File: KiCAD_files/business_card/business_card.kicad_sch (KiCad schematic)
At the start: 74 parts, among them J1 USB_C_Receptacle_USB2.0_14P, SW1 SW_MEC_5G, SW2 SW_MEC_5G, SW3 SW_MEC_5G, SW4 SW_MEC_5G, SW5 SW_MEC_5G, SW6 SW_MEC_5G, SW7 SW_MEC_5G, SW8 SW_MEC_5G, U1 STM32U073CCUx, U2 MCP1700x-300xxTT, U3 TPS3839DBZ

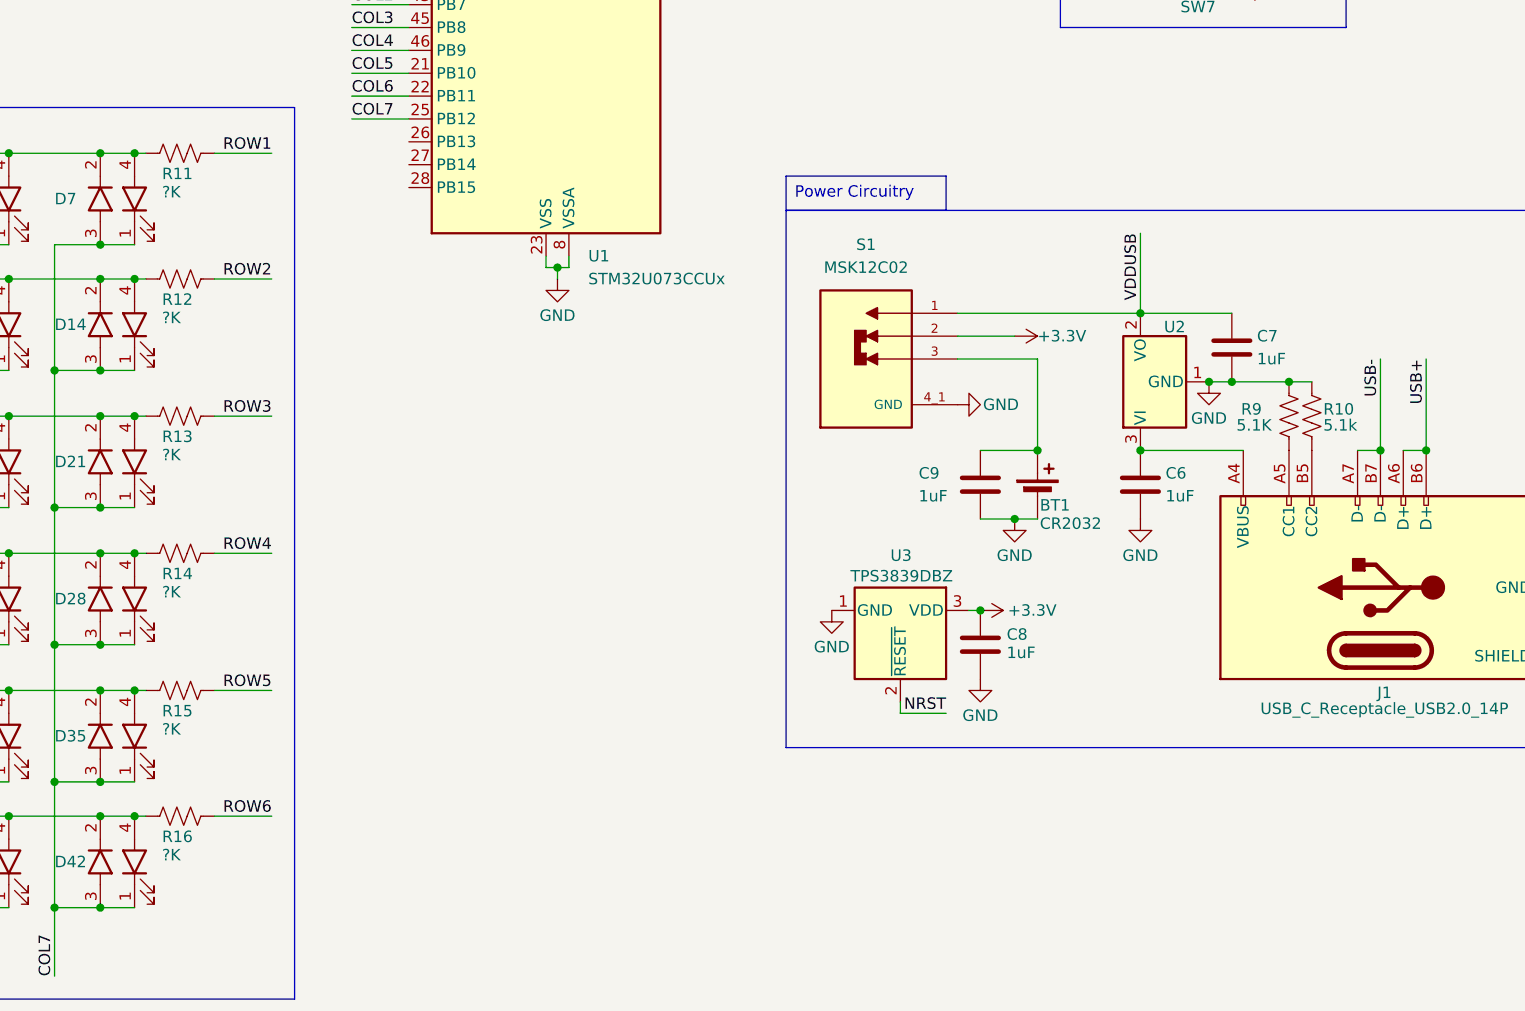
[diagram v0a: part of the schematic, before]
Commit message: Clean Up Files and Add Footprints
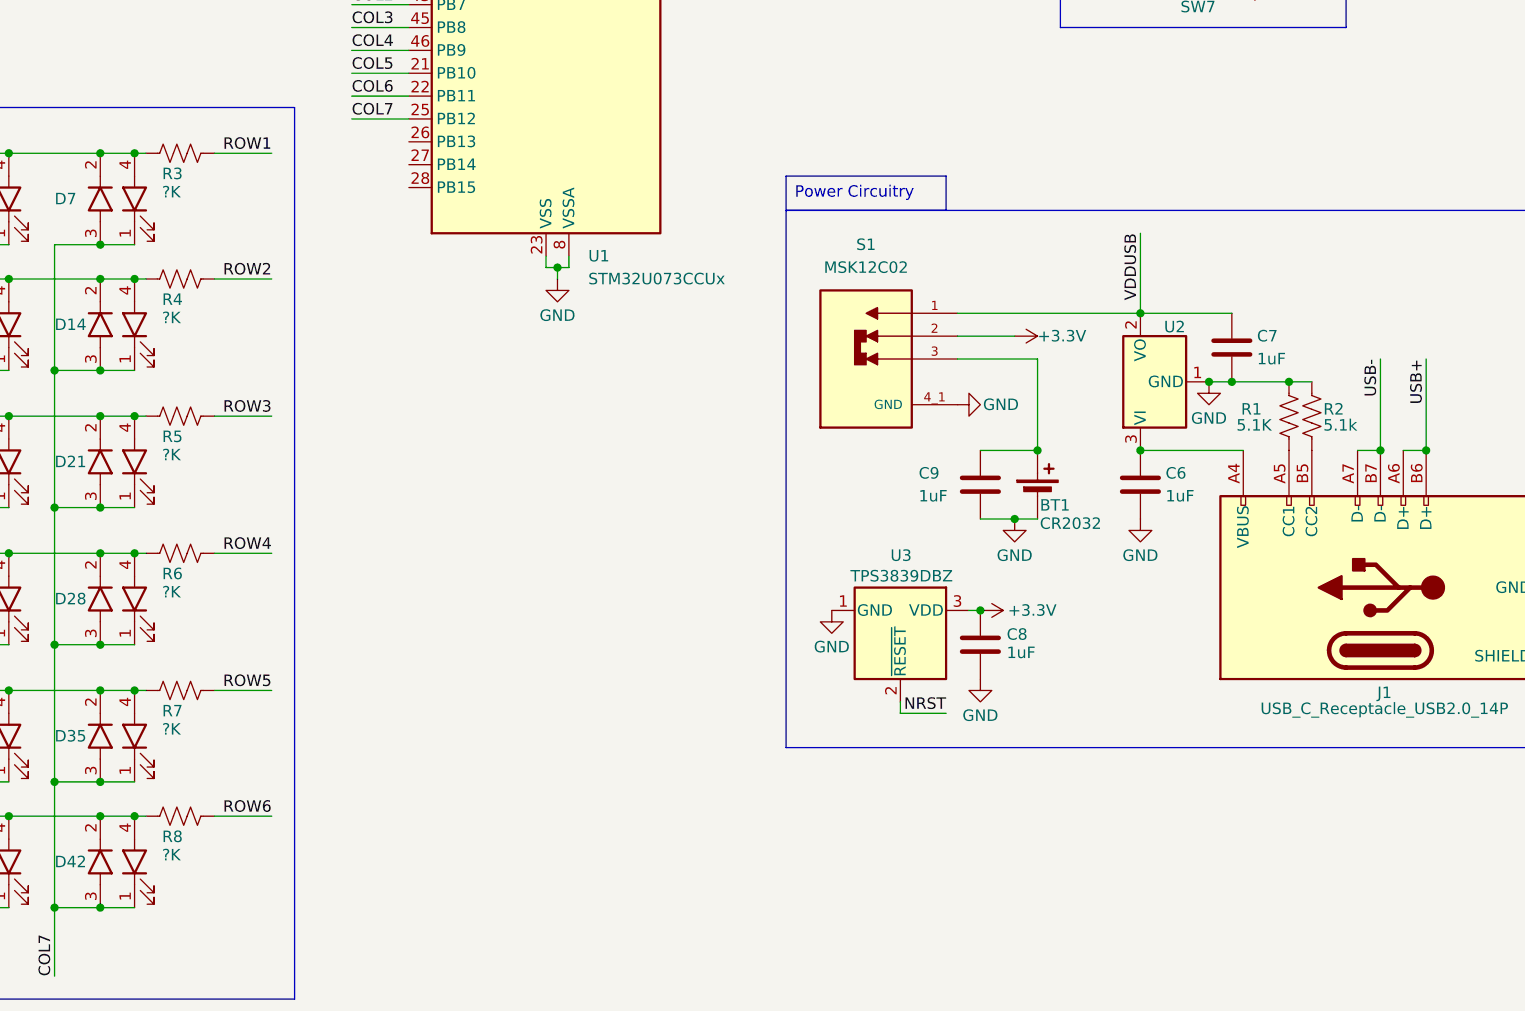
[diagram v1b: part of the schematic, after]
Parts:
- BT1: footprint (none) -> Battery:BatteryHolder_Keystone_3002_1x2032
- C1, C2, C3, C4, C5, C6, C7, C8, C9: footprint (none) -> Capacitor_SMD:C_0603_1608Metric
- R1: renamed from R9; footprint (none) -> Resistor_SMD:R_0603_1608Metric
- R2: renamed from R10; footprint (none) -> Resistor_SMD:R_0603_1608Metric
- R3: renamed from R11; footprint (none) -> Resistor_SMD:R_0603_1608Metric
- R4: renamed from R12; footprint (none) -> Resistor_SMD:R_0603_1608Metric
- R5: renamed from R13; footprint (none) -> Resistor_SMD:R_0603_1608Metric
- R6: renamed from R14; footprint (none) -> Resistor_SMD:R_0603_1608Metric
- R7: renamed from R15; footprint (none) -> Resistor_SMD:R_0603_1608Metric
- R8: renamed from R16; footprint (none) -> Resistor_SMD:R_0603_1608Metric
- SW1, SW2, SW3, SW4, SW5, SW6, SW7: footprint (none) -> custom_footprints:TSB008A2518A
- SW8: footprint (none) -> custom_footprints:TVAF06-N020C2-R
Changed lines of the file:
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@@
 			)
 		)
-		(property "Footprint" ""
+		(property "Footprint" "custom_footprints:TSB008A2518A"
 			(at 233.68 73.66 0)
 			(effects
@@
 		(on_board yes)
 		(dnp no)
-		(property "Reference" "R15"
+		(property "Reference" "R7"
 			(at 118.618 158.496 90)
 			(effects
@@
 			)
 		)
-		(property "Footprint" ""
+		(property "Footprint" "Resistor_SMD:R_0603_1608Metric"
 			(at 120.904 155.194 90)
 			(effects
@@
 			(project "business_card"
 				(path "/16d1a3fe-4f2d-4eb3-9740-21c0af2e4feb"
-					(reference "R15")
+					(reference "R7")
 					(unit 1)
 				)
@@
 		(on_board yes)
 		(dnp no)
-		(property "Reference" "R11"
+		(property "Reference" "R3"
 			(at 118.618 98.806 90)
 			(effects
@@
 			)
 		)
-		(property "Footprint" ""
+		(property "Footprint" "Resistor_SMD:R_0603_1608Metric"
 			(at 120.904 95.504 90)
 			(effects
@@
 			(project "business_card"
 				(path "/16d1a3fe-4f2d-4eb3-9740-21c0af2e4feb"
-					(reference "R11")
+					(reference "R3")
 					(unit 1)
 				)
@@
 			)
 		)
-		(property "Footprint" ""
+		(property "Footprint" "Capacitor_SMD:C_0603_1608Metric"
 			(at 228.2952 137.16 0)
 			(effects
@@
 			)
 		)
-		(property "Footprint" ""
+		(property "Footprint" "custom_footprints:TSB008A2518A"
 			(at 233.68 48.26 0)
 			(effects
@@
 			)
 		)
-		(property "Footprint" ""
+		(property "Footprint" "custom_footprints:TSB008A2518A"
 			(at 233.68 41.91 0)
 			(effects
@@
 			)
 		)
-		(property "Footprint" ""
+		(property "Footprint" "Capacitor_SMD:C_0603_1608Metric"
 			(at 210.5152 137.16 0)
 			(effects
@@
 			)
 		)
-		(property "Footprint" ""
+		(property "Footprint" "Capacitor_SMD:C_0603_1608Metric"
 			(at 208.5848 147.32 0)
 			(effects
@@
 			)
 		)
-		(property "Footprint" ""
+		(property "Footprint" "custom_footprints:TVAF06-N020C2-R"
 			(at 132.08 41.91 0)
 			(effects
@@
 			)
 		)
-		(property "Footprint" ""
+		(property "Footprint" "custom_footprints:TSB008A2518A"
 			(at 233.68 35.56 0)
 			(effects
@@
 			)
 		)
-		(property "Footprint" ""
+		(property "Footprint" "Battery:BatteryHolder_Keystone_3002_1x2032"
 			(at 215.9 133.096 90)
 			(effects
@@
 			)
 		)
-		(property "Footprint" ""
+		(property "Footprint" "custom_footprints:TSB008A2518A"
 			(at 233.68 54.61 0)
 			(effects
@@
 			)
 		)
-		(property "Footprint" ""
+		(property "Footprint" "Capacitor_SMD:C_0603_1608Metric"
 			(at 238.4552 121.92 0)
 			(effects
@@
 			)
 		)
-		(property "Footprint" ""
+		(property "Footprint" "Capacitor_SMD:C_0603_1608Metric"
 			(at 82.2452 39.37 0)
 			(effects
@@
 		(on_board yes)
 		(dnp no)
-		(property "Reference" "R14"
+		(property "Reference" "R6"
 			(at 118.618 143.256 90)
 			(effects
@@
 			)
 		)
-		(property "Footprint" ""
+		(property "Footprint" "Resistor_SMD:R_0603_1608Metric"
 			(at 120.904 139.954 90)
 			(effects
@@
 			(project "business_card"
 				(path "/16d1a3fe-4f2d-4eb3-9740-21c0af2e4feb"
-					(reference "R14")
+					(reference "R6")
 					(unit 1)
 				)
@@
 			)
 		)
-		(property "Footprint" ""
+		(property "Footprint" "custom_footprints:TSB008A2518A"
 			(at 233.68 60.96 0)
 			(effects
@@
 		(on_board yes)
 		(dnp no)
-		(property "Reference" "R12"
+		(property "Reference" "R4"
 			(at 118.618 112.776 90)
 			(effects
@@
 			)
 		)
-		(property "Footprint" ""
+		(property "Footprint" "Resistor_SMD:R_0603_1608Metric"
 			(at 120.904 109.474 90)
 			(effects
@@
 			(project "business_card"
 				(path "/16d1a3fe-4f2d-4eb3-9740-21c0af2e4feb"
-					(reference "R12")
+					(reference "R4")
 					(unit 1)
 				)
@@
 		(on_board yes)
 		(dnp no)
-		(property "Reference" "R13"
+		(property "Reference" "R5"
 			(at 118.618 128.016 90)
 			(effects
@@
 			)
 		)
-		(property "Footprint" ""
+		(property "Footprint" "Resistor_SMD:R_0603_1608Metric"
 			(at 120.904 124.714 90)
 			(effects
@@
 			(project "business_card"
 				(path "/16d1a3fe-4f2d-4eb3-9740-21c0af2e4feb"
-					(reference "R13")
+					(reference "R5")
 					(unit 1)
 				)
@@
 			)
 		)
-		(property "Footprint" ""
+		(property "Footprint" "custom_footprints:TSB008A2518A"
 			(at 233.68 67.31 0)
 			(effects
@@
 			)
 		)
-		(property "Footprint" ""
+		(property "Footprint" "Capacitor_SMD:C_0603_1608Metric"
 			(at 72.0852 39.37 0)
 			(effects
@@
 		(on_board yes)
 		(dnp no)
-		(property "Reference" "R16"
+		(property "Reference" "R8"
 			(at 118.618 172.466 90)
 			(effects
@@
 			)
 		)
-		(property "Footprint" ""
+		(property "Footprint" "Resistor_SMD:R_0603_1608Metric"
 			(at 120.904 169.164 90)
 			(effects
@@
 			(project "business_card"
 				(path "/16d1a3fe-4f2d-4eb3-9740-21c0af2e4feb"
-					(reference "R16")
+					(reference "R8")
 					(unit 1)
 				)
@@
 		(on_board yes)
 		(dnp no)
-		(property "Reference" "R9"
+		(property "Reference" "R1"
 			(at 238.506 124.968 0)
 			(effects
@@
 			)
 		)
-		(property "Footprint" ""
+		(property "Footprint" "Resistor_SMD:R_0603_1608Metric"
 			(at 244.856 125.984 90)
 			(effects
@@
 			(project "business_card"
 				(path "/16d1a3fe-4f2d-4eb3-9740-21c0af2e4feb"
-					(reference "R9")
+					(reference "R1")
 					(unit 1)
 				)
@@
 		(on_board yes)
 		(dnp no)
-		(property "Reference" "R10"
+		(property "Reference" "R2"
 			(at 247.65 124.968 0)
 			(effects
@@
 			)
 		)
-		(property "Footprint" ""
+		(property "Footprint" "Resistor_SMD:R_0603_1608Metric"
 			(at 247.396 125.984 90)
 			(effects
@@
 			(project "business_card"
 				(path "/16d1a3fe-4f2d-4eb3-9740-21c0af2e4feb"
-					(reference "R10")
+					(reference "R2")
 					(unit 1)
 				)
@@
 			)
 		)
-		(property "Footprint" ""
+		(property "Footprint" "Capacitor_SMD:C_0603_1608Metric"
 			(at 35.2552 39.37 0)
 			(effects
@@
 			)
 		)
-		(property "Footprint" ""
+		(property "Footprint" "Capacitor_SMD:C_0603_1608Metric"
 			(at 58.1152 39.37 0)
 			(effects
@@
 			)
 		)
-		(property "Footprint" ""
+		(property "Footprint" "Capacitor_SMD:C_0603_1608Metric"
 			(at 46.6852 39.37 0)
 			(effects

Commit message: Add Debug Interface and Test Points
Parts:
- added J2: Conn_01x05_Pin, symbol Connector:Conn_01x05_Pin
- added TP1: VDDUSB, symbol Connector:TestPoint
- added TP2: VDDBAT, symbol Connector:TestPoint
- added TP3: VDD, symbol Connector:TestPoint
- added TP4: GND, symbol Connector:TestPoint
- added TP5: USB-, symbol Connector:TestPoint
- added TP6: USB+, symbol Connector:TestPoint
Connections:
- net +3.3V: now also J2.1 (Pin_1), TP3.1
- net GND: now also J2.5 (Pin_5), TP4.1
- net NRST: now also J2.2 (Pin_2)
- net SWCLK: now also J2.4 (Pin_4)
- net SWDIO: now also J2.3 (Pin_3)
- net USB+: now also TP6.1
- net USB-: now also TP5.1
- net VDDUSB: now also TP1.1
- net at BT1.1 (+), C9.1, S1.3: now also TP2.1
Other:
- moved on the sheet: BT1, C9

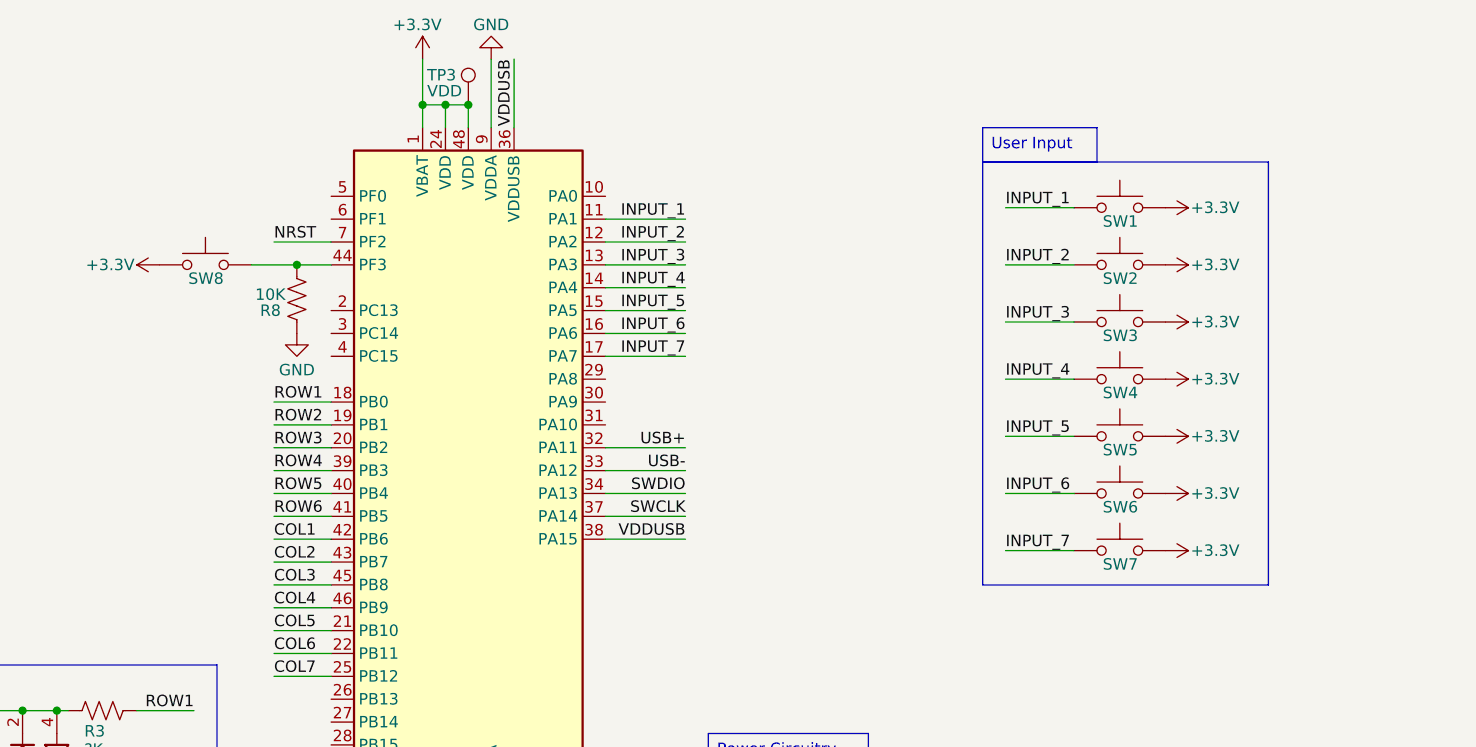
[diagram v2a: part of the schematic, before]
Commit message: Update Footprints of Components and Start Layout Design
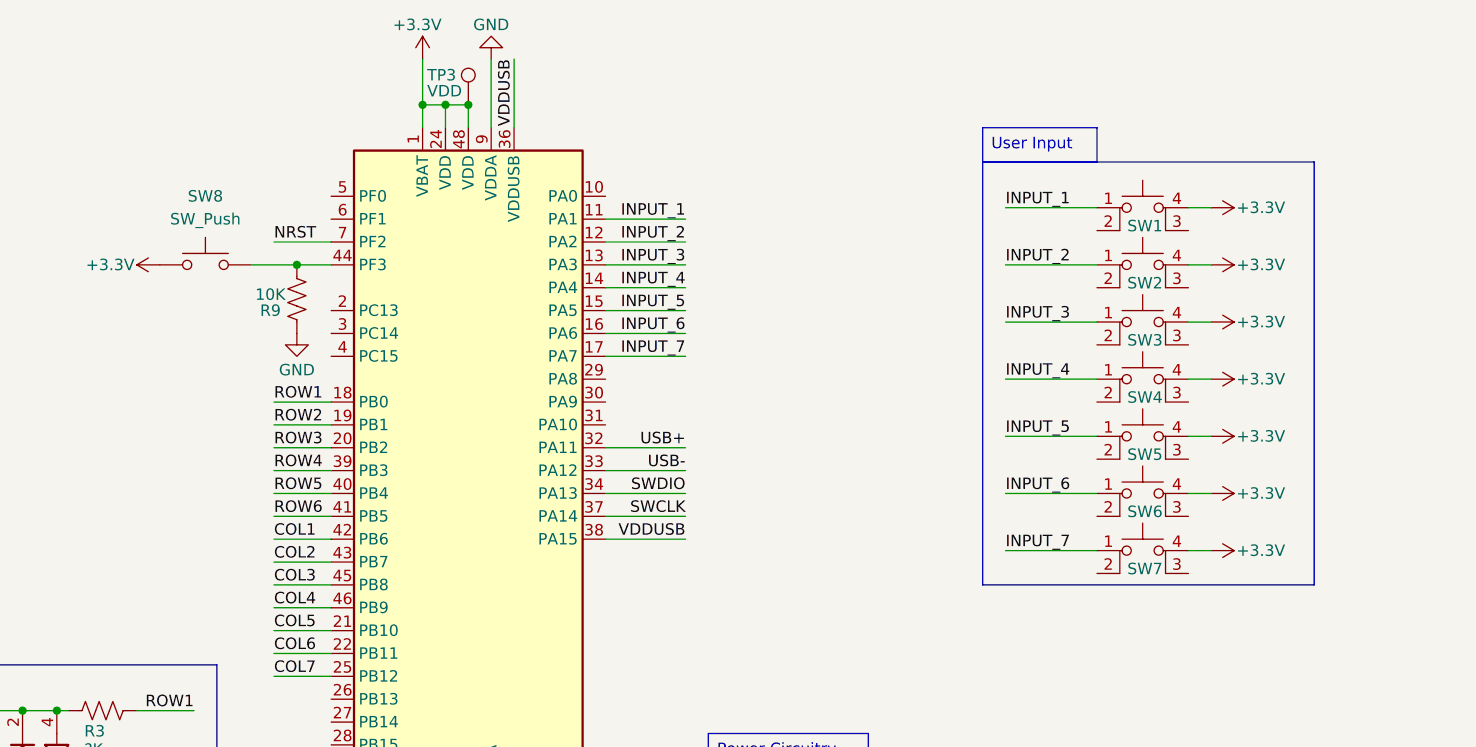
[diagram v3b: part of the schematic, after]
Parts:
- removed SW1, SW2, SW3, SW4, SW5, SW6, SW7: SW_MEC_5G, custom_footprints:TSB008A2518A, symbol Switch:SW_MEC_5G
- removed SW8: SW_MEC_5G, custom_footprints:TVAF06-N020C2-R, symbol Switch:SW_MEC_5G
- added SW1, SW2, SW3, SW4, SW5, SW6, SW7: SW_MEC_5E, 1TS026A-2000-0553-CT:SW-SMD_4P-L2.6-W1.6-P0.75-LS3.0, symbol Switch:SW_MEC_5E
- added SW8: SW_Push, TSB008A2526A:TSB008A2526A, symbol Switch:SW_Push
- D1, D10, D11, D12, D13, D14, D15, D16, D17, D18, D19, D2, D20, D21, D22, D23, D24, D25, D26, D27, D28, D29, D3, D30, D31, D32, D33, D34, D35, D36, D37, D38, D39, D4, D40, D41, D42, D5, D6, D7, D8, D9: footprint (none) -> P4-1615ROTCA1-0.6T_same_size:LED_CHIP
- J1: footprint (none) -> USB-C-SMD_TYPE-C-6PIN-2MD-073:USB-C-SMD_TYPE-C-6PIN-2MD-073
- J2: footprint (none) -> Connector_PinHeader_1.00mm:PinHeader_1x05_P1.00mm_Vertical
- R9: renamed from R8; footprint (none) -> Resistor_SMD:R_0603_1608Metric
- TP1, TP2, TP3, TP4, TP5, TP6: footprint (none) -> TestPoint:TestPoint_THTPad_D1.0mm_Drill0.5mm
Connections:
- net +3.3V: now also SW1.4 (A), SW2.4 (A), SW3.4 (A), SW4.4 (A), SW5.4 (A), SW6.4 (A), SW7.4 (A), SW8.1
- net INPUT_1: now also SW1.1
- net INPUT_2: now also SW2.1
- net INPUT_3: now also SW3.1
- net INPUT_4: now also SW4.1
- net INPUT_5: now also SW5.1
- net INPUT_6: now also SW6.1
- net INPUT_7: now also SW7.1
- net at R9.1, U1.44 (PF3): now also SW8.2
